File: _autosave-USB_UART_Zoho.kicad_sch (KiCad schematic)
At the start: 21 parts, among them J2 Peripherals, J3 USB3_A, J4 VccIo_jumper, U1 FT232RL, U2 USBLC6-2P6

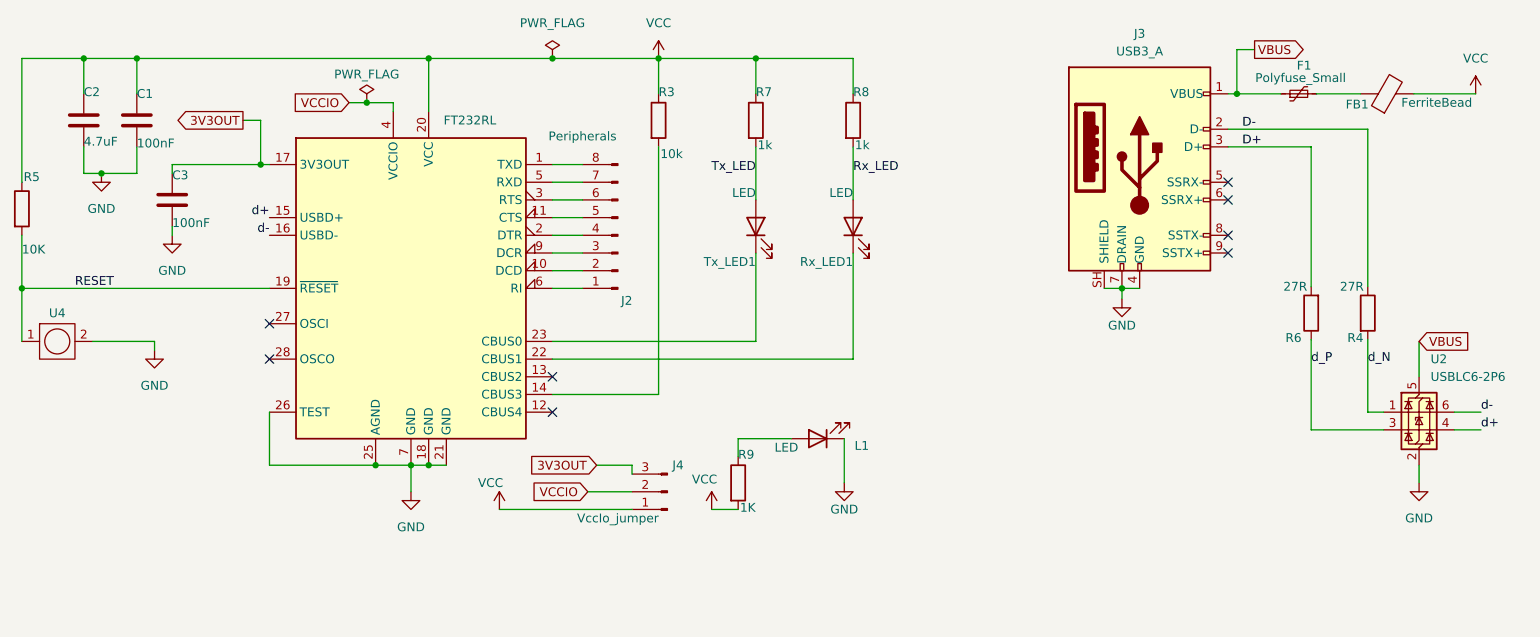
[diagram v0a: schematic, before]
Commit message: USB type C changed to USB type A: some desgin changes in the routing
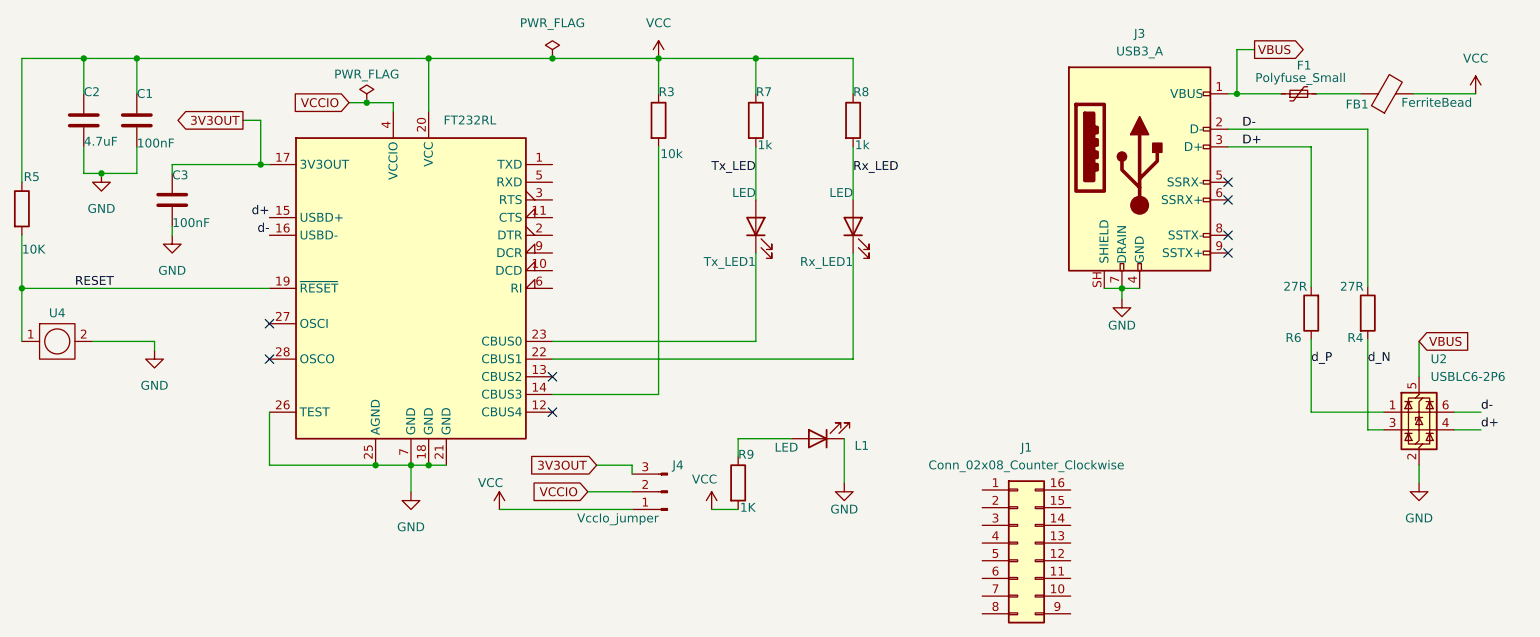
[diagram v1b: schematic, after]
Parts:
- removed J2: Peripherals, Connector_PinHeader_2.54mm:PinHeader_1x08_P2.54mm_Horizontal, symbol Connector:Conn_01x08_Pin
- added J1: Conn_02x08_Counter_Clockwise, Connector_PinSocket_2.00mm:PinSocket_2x08_P2.00mm_Horizontal, symbol Connector_Generic:Conn_02x08_Counter_Clockwise
- U4: footprint Button_Switch_THT:SW_PUSH_6mm_H5mm -> Button_Switch_SMD:SW_Push_SPST_NO_Alps_SKRK
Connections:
- net d_N: now also U2.3 (I/O2); no longer U2.1 (I/O1)
- net d_P: now also U2.1 (I/O1); no longer U2.3 (I/O2)
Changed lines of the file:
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@@
 	(wire
 		(pts
-			(xy 235.204 107.696) (xy 235.204 118.11)
+			(xy 235.204 107.696) (xy 235.204 120.65)
 		)
 		(stroke
@@
 	(wire
 		(pts
-			(xy 122.428 100.33) (xy 118.11 100.33)
-		)
-		(stroke
-			(width 0)
-			(type default)
-		)
-	)
-	(wire
-		(pts
 			(xy 41.91 100.33) (xy 77.47 100.33)
 		)
@@
 	(wire
 		(pts
-			(xy 227.076 120.65) (xy 237.49 120.65)
-		)
-		(stroke
-			(width 0)
-			(type default)
-		)
-	)
-	(wire
-		(pts
 			(xy 133.35 80.01) (xy 133.35 115.57)
 		)
@@
 	(wire
 		(pts
-			(xy 122.428 82.55) (xy 118.11 82.55)
+			(xy 235.204 120.65) (xy 237.49 120.65)
 		)
 		(stroke
@@
 	(wire
 		(pts
-			(xy 122.428 87.63) (xy 118.11 87.63)
+			(xy 227.076 118.11) (xy 237.49 118.11)
 		)
 		(stroke
@@
 	(wire
 		(pts
-			(xy 122.428 90.17) (xy 118.11 90.17)
-		)
-		(stroke
-			(width 0)
-			(type default)
-		)
-	)
-	(wire
-		(pts
 			(xy 144.78 121.92) (xy 144.78 124.46)
 		)
@@
 	(wire
 		(pts
-			(xy 235.204 118.11) (xy 237.49 118.11)
-		)
-		(stroke
-			(width 0)
-			(type default)
-		)
-	)
-	(wire
-		(pts
-			(xy 122.428 97.79) (xy 118.11 97.79)
-		)
-		(stroke
-			(width 0)
-			(type default)
-		)
-	)
-	(wire
-		(pts
 			(xy 199.898 101.854) (xy 199.898 100.33)
 		)
@@
 	(wire
 		(pts
-			(xy 122.428 95.25) (xy 118.11 95.25)
-		)
-		(stroke
-			(width 0)
-			(type default)
-		)
-	)
-	(wire
-		(pts
 			(xy 110.49 132.08) (xy 129.54 132.08)
 		)
@@
 	(wire
 		(pts
-			(xy 122.428 92.71) (xy 118.11 92.71)
-		)
-		(stroke
-			(width 0)
-			(type default)
-		)
-	)
-	(wire
-		(pts
 			(xy 92.71 125.73) (xy 97.79 125.73)
 		)
@@
 	(wire
 		(pts
-			(xy 227.076 107.696) (xy 227.076 120.65)
+			(xy 227.076 107.696) (xy 227.076 118.11)
 		)
 		(stroke
@@
 	(wire
 		(pts
-			(xy 122.428 85.09) (xy 118.11 85.09)
-		)
-		(stroke
-			(width 0)
-			(type default)
-		)
-	)
-	(wire
-		(pts
 			(xy 41.91 85.09) (xy 41.91 67.31)
 		)
@@
 			)
 		)
-		(property "Footprint" "Button_Switch_THT:SW_PUSH_6mm_H5mm"
+		(property "Footprint" "Button_Switch_SMD:SW_Push_SPST_NO_Alps_SKRK"
 			(at 46.99 107.95 0)
 			(hide yes)
@@
 	)
 	(symbol
-		(lib_id "Connector:Conn_01x08_Pin")
-		(at 127.508 92.71 180)
-		(unit 1)
-		(body_style 1)
-		(exclude_from_sim no)
-		(in_bom yes)
-		(on_board yes)
-		(in_pos_files yes)
-		(dnp no)
-		(property "Reference" "J2"
-			(at 128.778 102.108 0)
-			(show_name no)
-			(do_not_autoplace no)
-			(effects
-				(font
-					(size 1.27 1.27)
-				)
-			)
-		)
-		(property "Value" "Peripherals"
-			(at 122.428 78.486 0)
-			(show_name no)
-			(do_not_autoplace no)
-			(effects
-				(font
-					(size 1.27 1.27)
-				)
-			)
-		)
-		(property "Footprint" "Connector_PinHeader_2.54mm:PinHeader_1x08_P2.54mm_Horizontal"
-			(at 127.508 92.71 0)
-			(hide yes)
-			(show_name no)
-			(do_not_autoplace no)
-			(effects
-				(font
-					(size 1.27 1.27)
-				)
-			)
-		)
-		(property "Datasheet" ""
-			(at 127.508 92.71 0)
-			(hide yes)
-			(show_name no)
-			(do_not_autoplace no)
-			(effects
-				(font
-					(size 1.27 1.27)
-				)
-			)
-		)
-		(property "Description" "Generic connector, single row, 01x08, script generated"
-			(at 127.508 92.71 0)
-			(hide yes)
-			(show_name no)
-			(do_not_autoplace no)
-			(effects
-				(font
-					(size 1.27 1.27)
-				)
-			)
-		)
-		(pin "4"
-		)
-		(pin "3"
-		)
-		(pin "2"
-		)
-		(pin "1"
-		)
-		(pin "6"
-		)
-		(pin "7"
-		)
-		(pin "5"
-		)
-		(pin "8"
-		)
-		(instances
-			(project "USB_UART_Zoho"
-				(path "/04430ea8-bdcd-4b4a-bfd9-16e0e9121bf7"
-					(reference "J2")
-					(unit 1)
-				)
-			)
-		)
-	)
-	(symbol
 		(lib_id "power:GND")
 		(at 97.79 129.54 0)
@@
 					(unit 1)
 				)
+			)
+		)
+	)
+	(symbol
+		(lib_id "Connector_Generic:Conn_02x08_Counter_Clockwise")
+		(at 184.912 136.906 0)
+		(unit 1)
+		(body_style 1)
+		(exclude_from_sim no)
+		(in_bom yes)
+		(on_board yes)
+		(in_pos_files yes)
+		(dnp no)
+		(fields_autoplaced yes)
+		(property "Reference" "J1"
+			(at 186.182 123.19 0)
+			(show_name no)
+			(do_not_autoplace no)
+			(effects
+				(font
+					(size 1.27 1.27)
+				)
+			)
+		)
+		(property "Value" "Conn_02x08_Counter_Clockwise"
+			(at 186.182 125.73 0)
+			(show_name no)
+			(do_not_autoplace no)
+			(effects
+				(font
+					(size 1.27 1.27)
+				)
+			)
+		)
+		(property "Footprint" "Connector_PinSocket_2.00mm:PinSocket_2x08_P2.00mm_Horizontal"
+			(at 184.912 136.906 0)
+			(hide yes)
+			(show_name no)
+			(do_not_autoplace no)
+			(effects
+				(font
+					(size 1.27 1.27)
+				)
+			)
+		)
+		(property "Datasheet" ""
+			(at 184.912 136.906 0)
+			(hide yes)
+			(show_name no)
+			(do_not_autoplace no)
+			(effects
+				(font
+					(size 1.27 1.27)
+				)
+			)
+		)
+		(property "Description" "Generic connector, double row, 02x08, counter clockwise pin numbering scheme (similar to DIP package numbering), script generated (kicad-library-utils/schlib/autogen/connector/)"
+			(at 184.912 136.906 0)
+			(hide yes)
+			(show_name no)
+			(do_not_autoplace no)
+			(effects
+				(font
+					(size 1.27 1.27)
+				)
+			)
+		)
+		(pin "9"
+		)
+		(pin "10"
+		)
+		(pin "15"
+		)
+		(pin "2"
+		)
+		(pin "7"
+		)
+		(pin "1"
+		)
+		(pin "4"
+		)
+		(pin "6"
+		)
+		(pin "8"
+		)
+		(pin "14"
+		)
+		(pin "16"
+		)
+		(pin "13"
+		)
+		(pin "5"
+		)
+		(pin "12"
+		)
+		(pin "11"
+		)
+		(pin "3"
+		)
+		(instances
+			(project "USB_UART_Zoho"
+				(path "/04430ea8-bdcd-4b4a-bfd9-16e0e9121bf7"
+					(reference "J1")
+					(unit 1)
+				)
